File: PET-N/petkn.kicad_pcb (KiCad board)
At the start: 2 copper layers, 386.1 x 102 mm, 110 parts, among them J1 Extended_PET_keyboard_connect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, J4 AVR-ISP-6, J7 AVR-ISP-6, SW1 KP "=", SW10 KP "0", SW11 R SHIFT, SW12 ">", SW14 "]", SW15 "@", SW16 L SHIFT, SW17 KP "+", SW18 KP "2", SW2 KP ".", SW20 "?", SW21 ",", SW22 "N", SW23 "V", SW24 "X", SW25 KP "3", SW26 KP "1", SW27 RETURN, SW28 ";", SW29 "M", SW3 NC ($10), SW30 "B", SW31 "C", SW32 "Z", SW320 S LOCK, SW33 KP "*", SW34 KP "5", SW36 ":", SW37 "K", SW38 "H", SW39 "F", SW4 STOP, SW40 "S", SW41 KP "6", SW42 KP "4", SW44 "L", SW45 "J", SW46 "G", SW47 "D", SW48 "A", SW49 KP "/", SW5 "<", SW50 KP "8", SW52 "P", SW53 "I", SW54 "Y", SW55 "R", SW56 "W", SW57 KP "9", SW58 KP "7", SW59 U ARROW, SW6 SPACE, SW60 "O", SW61 "U", SW62 "T", SW63 "E", SW64 "Q", SW65 INS/DEL, SW66 UP/DOWN, SW67 NC ($0A), SW68 ")", SW69 "\", SW7 "[", SW70 "'", SW71 "$", SW72 QUOTE, SW73 LEFT/RIGHT, SW74 CLR/HOME, SW75 B ARROW, SW76 "(", SW77 "&", SW78 "%", SW79 "#", SW8 OFF/RVS, SW80 "!", SW9 KP "-", U1 LSF0204Q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

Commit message: layout work
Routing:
- net C6: track 135.7 -> 462.6 mm, vias 2 -> 5
- net C3: track 152.8 -> 469.9 mm, vias 3 -> 8
- net R10: track 122.7 -> 415.3 mm, vias 2 -> 10
- net C1: track 245.8 -> 516.1 mm, vias 4 -> 7
- net Net-(SW67B-DOUT): track 0.00 -> 241.9 mm, vias 0 -> 4
- net cR1: track 55.9 -> 279.1 mm, vias 3 -> 5
- net R2: track 170.4 -> 388.5 mm, vias 0 -> 1
- net Net-(SW59B-DOUT): track 0.00 -> 216.3 mm, vias 0 -> 4
- net Net-(SW14B-DIN): track 0.00 -> 211.3 mm, vias 0 -> 4
- net L5: track 0.00 -> 200.2 mm, vias 0 -> 4
- net LVSDA: track 0.00 -> 187.2 mm, vias 0 -> 3
- net C8: track 171.5 -> 350.2 mm, vias 0 -> 1
- net LVSCL: track 0.00 -> 176.6 mm, vias 0 -> 3
- net VCC33: track 10.2 -> 182.7 mm, vias 0 -> 3
- net R1: track 159.0 -> 325.2 mm
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
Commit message: petn layout work
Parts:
- moved C7 5.54 mm to (280.1, 135.3), turned to 180 degrees
- moved C17 1.84 mm to (279.9, 138.7)
- moved JP4 0.73 mm to (64.0, 141.7)
- turned Y1 to 180 degrees
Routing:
- net GND: track 1449.1 -> 2438.3 mm, vias 6 -> 63
- net C2: track 302.6 -> 476.0 mm, vias 4 -> 5
- net R3: track 286.0 -> 456.7 mm, vias 1 -> 4
- net R10: track 415.3 -> 585.8 mm, vias 10 -> 13
- net R6: track 249.8 -> 411.3 mm, vias 1 -> 6
- net VCC: track 1738.7 -> 1898.4 mm, vias 18 -> 25
- net R7: track 270.0 -> 408.7 mm, vias 0 -> 4
- net R9: track 466.6 -> 602.3 mm, vias 4 -> 8
- net C4: track 359.0 -> 493.7 mm, vias 6 -> 9
- net R2: track 388.5 -> 522.0 mm
- net L0: track 0.00 -> 127.2 mm, vias 0 -> 2
- net L2: track 0.00 -> 119.5 mm, vias 0 -> 2
- net R1: track 325.2 -> 435.6 mm, vias 0 -> 4
- net C5: track 183.3 -> 290.6 mm, vias 4 -> 9
- net L1: track 0.00 -> 91.7 mm, vias 0 -> 2
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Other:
- board text removed: "SW3=SPACE"

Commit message: more layout work
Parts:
- added C1: 100u, Capacitor_SMD:C_1206_3216Metric_Pad1.33x1.80mm_HandSolder, B.Cu at (165.5, 83.8)
- added C19: 100u, Capacitor_SMD:C_1206_3216Metric_Pad1.33x1.80mm_HandSolder, B.Cu at (238.0, 121.3)
- added C2: 100u, Capacitor_SMD:C_1206_3216Metric_Pad1.33x1.80mm_HandSolder, B.Cu at (170.6, 102.8)
- added C20: 100u, Capacitor_SMD:C_1206_3216Metric_Pad1.33x1.80mm_HandSolder, B.Cu at (156.3, 64.6)
- added C21: 100u, Capacitor_SMD:C_1206_3216Metric_Pad1.33x1.80mm_HandSolder, B.Cu at (98.5, 64.0)
- added C22: 100u, Capacitor_SMD:C_1206_3216Metric_Pad1.33x1.80mm_HandSolder, B.Cu at (108.1, 83.0)
- added C23: 100u, Capacitor_SMD:C_1206_3216Metric_Pad1.33x1.80mm_HandSolder, B.Cu at (113.7, 102.0)
- added C24: 100u, Capacitor_SMD:C_1206_3216Metric_Pad1.33x1.80mm_HandSolder, B.Cu at (103.0, 121.8)
- added C25: 100u, Capacitor_SMD:C_1206_3216Metric_Pad1.33x1.80mm_HandSolder, B.Cu at (333.6, 63.8)
- added C26: 100u, Capacitor_SMD:C_1206_3216Metric_Pad1.33x1.80mm_HandSolder, B.Cu at (333.5, 83.0)
- added C27: 100u, Capacitor_SMD:C_1206_3216Metric_Pad1.33x1.80mm_HandSolder, B.Cu at (333.6, 102.3)
- added C28: 100u, Capacitor_SMD:C_1206_3216Metric_Pad1.33x1.80mm_HandSolder, B.Cu at (332.5, 121.1)
- added C29: 100u, Capacitor_SMD:C_1206_3216Metric_Pad1.33x1.80mm_HandSolder, B.Cu at (333.0, 140.6)
- added C3: 100u, Capacitor_SMD:C_1206_3216Metric_Pad1.33x1.80mm_HandSolder, B.Cu at (161.0, 121.3)
- added C4: 100u, Capacitor_SMD:C_1206_3216Metric_Pad1.33x1.80mm_HandSolder, B.Cu at (251.3, 64.1)
- added C5: 100u, Capacitor_SMD:C_1206_3216Metric_Pad1.33x1.80mm_HandSolder, B.Cu at (242.0, 83.7)
- added C6: 100u, Capacitor_SMD:C_1206_3216Metric_Pad1.33x1.80mm_HandSolder, B.Cu at (247.1, 102.8)
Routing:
- net VCC: track 1898.4 -> 2735.0 mm, vias 25 -> 66
- net GND: track 2438.3 -> 2545.4 mm, vias 63 -> 81
- net C6: track 465.4 -> 468.2 mm
- net R8: track 401.9 -> 399.1 mm
- net R6: track 411.3 -> 409.4 mm
- net Net-(SW11B-DIN): track 70.0 -> 71.8 mm
- net Net-(SW67B-DOUT): track 247.2 -> 245.4 mm
- net C4: track 493.7 -> 495.4 mm
- net C1: track 518.5 -> 517.2 mm
- net Net-(SW61B-DOUT): track 49.2 -> 50.4 mm
- net L3: track 73.7 -> 74.8 mm
- net Net-(SW21B-DIN): track 200.2 -> 201.4 mm
- net R9: track 602.3 -> 603.5 mm, vias 8 -> 9
- net S3: track 183.0 -> 181.9 mm
- net VCC33: track 186.4 -> 185.5 mm
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
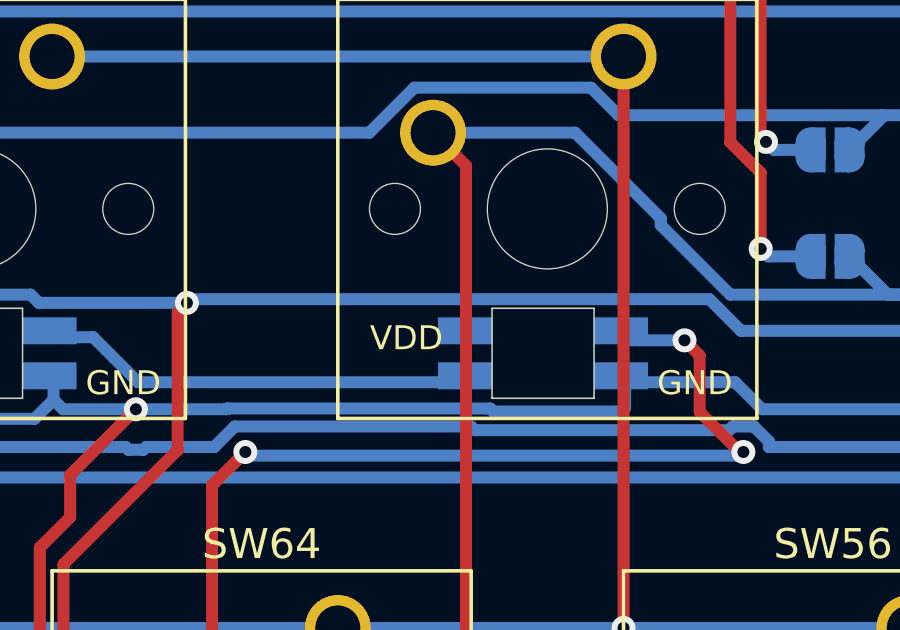
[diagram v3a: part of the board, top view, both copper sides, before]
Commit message: add missing pcb trace
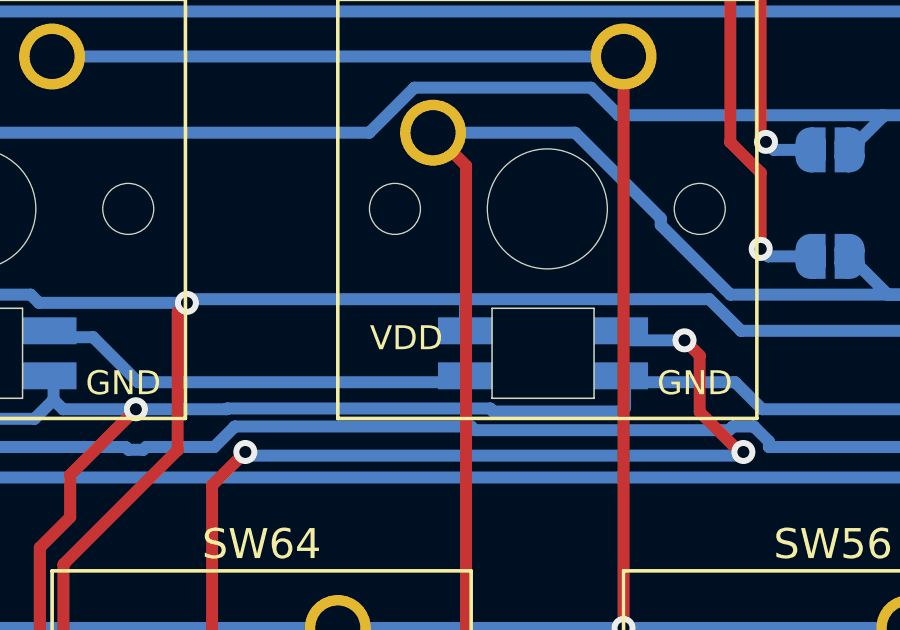
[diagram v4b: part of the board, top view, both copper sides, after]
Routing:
- net VCC: track 2735.0 -> 2736.1 mm
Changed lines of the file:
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@@
+	)
+	(segment
+		(start 67.8688 62.738)
+		(end 67.7672 62.6364)
+		(width 0.4)
+		(layer "B.Cu")
+		(net 35)
 	)
 	(segment
@@
 	)
 	(segment
+		(start 58.72063 62.6364)
+		(end 67.7672 62.6364)
+		(width 0.4)
+		(layer "B.Cu")
+		(net 35)
+	)
+	(segment
 		(start 279.4 94.488)
 		(end 281.826237 94.488)
@@
 	)
 	(segment
-		(start 58.72063 62.6364)
+		(start 67.7672 62.6364)
 		(end 76.01348 62.6364)
 		(width 0.4)
@@
 		(width 0.4)
 		(layer "B.Cu")
+		(net 35)
+	)
+	(segment
+		(start 67.8688 63.6905)
+		(end 67.8688 62.738)
+		(width 0.4)
+		(layer "B.Cu")

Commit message: almost done routing; last checks still open
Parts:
- added C30: 100n, Capacitor_SMD:C_0805_2012Metric_Pad1.18x1.45mm_HandSolder, B.Cu at (252.6, 136.4)
- added C31: 100n, Capacitor_SMD:C_0805_2012Metric_Pad1.18x1.45mm_HandSolder, B.Cu at (317.7, 101.1)
- added C32: 100u, Capacitor_SMD:C_1206_3216Metric_Pad1.33x1.80mm_HandSolder, B.Cu at (295.2, 92.9)
- added C33: 100u, Capacitor_SMD:C_1206_3216Metric_Pad1.33x1.80mm_HandSolder, B.Cu at (211.0, 136.2)
- added U5: ~, petkn:THB Miniature Thumbstick THB001P, F.Cu at (302.2, 135.0)
- moved C18 22.4 mm to (98.4, 136.2), turned to 90 degrees
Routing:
- net GND: track 2545.4 -> 2645.4 mm, vias 81 -> 86
- net R4: track 496.4 -> 560.0 mm, vias 4 -> 5
- net C6: track 468.2 -> 514.3 mm, vias 5 -> 6
- net R6: track 409.4 -> 445.9 mm, vias 6 -> 7
- net R5: track 452.4 -> 481.4 mm
- net R7: track 408.1 -> 425.4 mm, vias 4 -> 5
- net L2: track 119.8 -> 132.2 mm
- net R8: track 399.1 -> 407.2 mm, vias 4 -> 5
- net R10: track 585.9 -> 592.5 mm
- net C7: track 442.5 -> 447.0 mm
- net R9: track 603.5 -> 599.2 mm
- net CLK16M: track 232.5 -> 236.3 mm
- net Net-(U2-PD0): track 59.3 -> 62.1 mm
- net C5: track 290.6 -> 292.9 mm
- net Net-(U2-PD1): track 62.5 -> 64.7 mm
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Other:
- outline, holes or cut-outs redrawn
- board text added: "CBM-KEYB-PETN-3.0-20251005"
- board text added: "{dblquote}N-V3-R0{dblquote} (C) A. Fachat, 2025-10-05"
- board text removed: "{dblquote}N-V3{dblquote} (C) A. Fachat, 2025-08-12"
